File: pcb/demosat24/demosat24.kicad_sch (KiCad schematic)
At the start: 7 parts, among them J1 Power, J2 Digital/PWM, J3 Analog, J4 Digital/PWM, J5 Conn_01x04, J6 Conn_01x04, J7 Conn_01x02

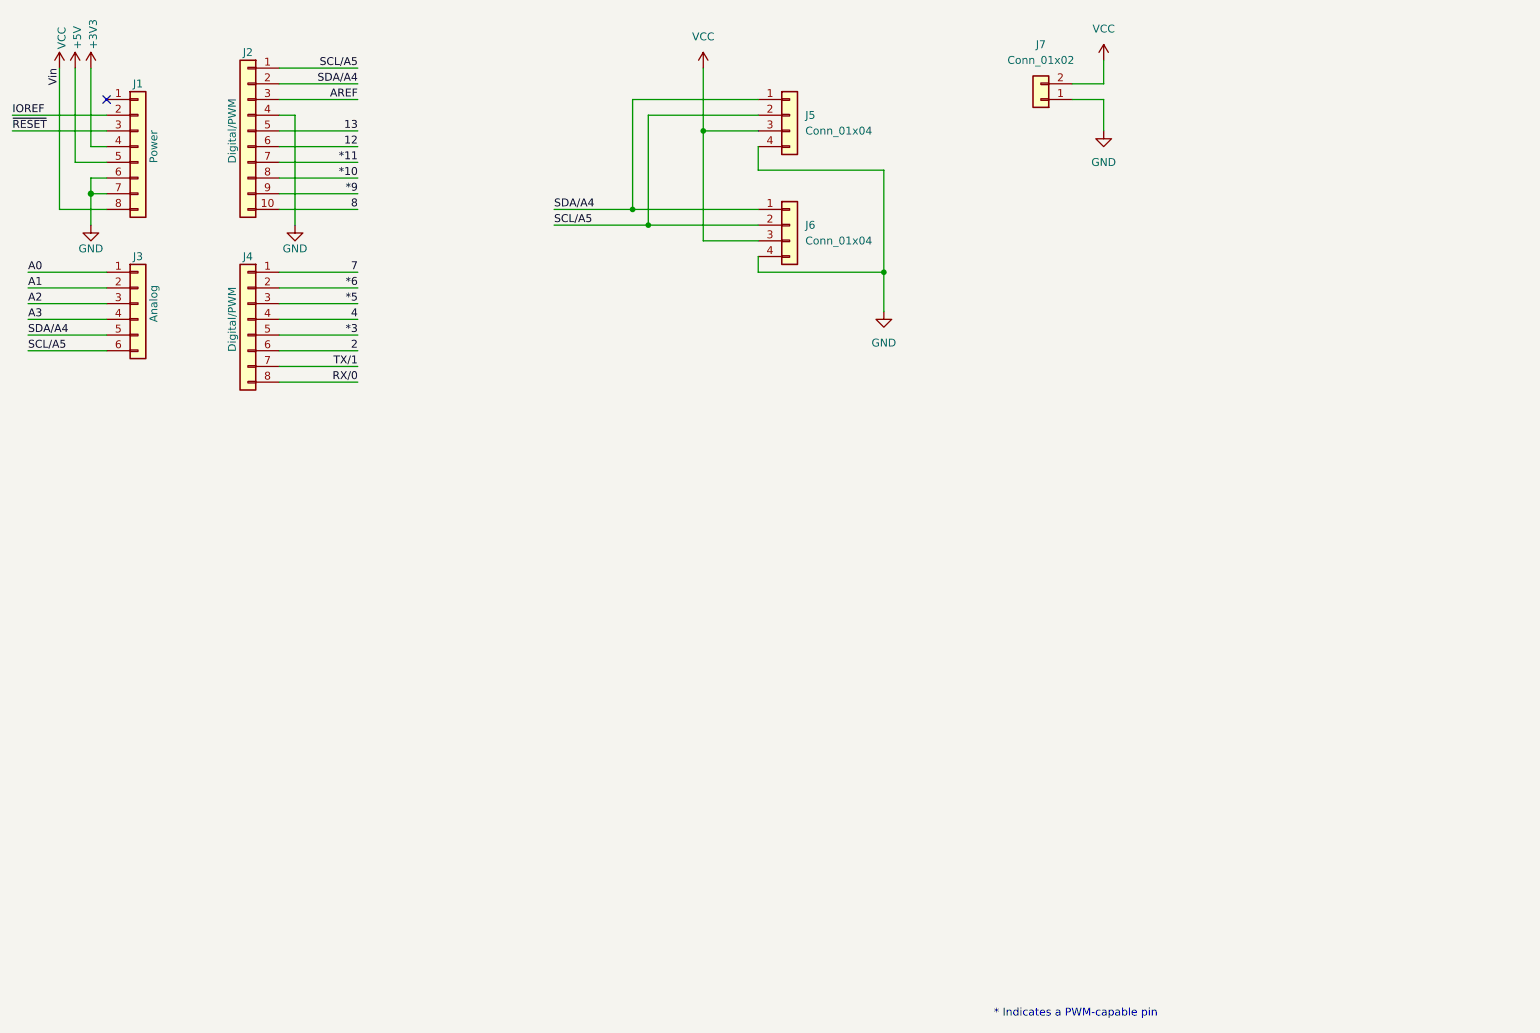
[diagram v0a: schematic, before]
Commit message: complete schematic added
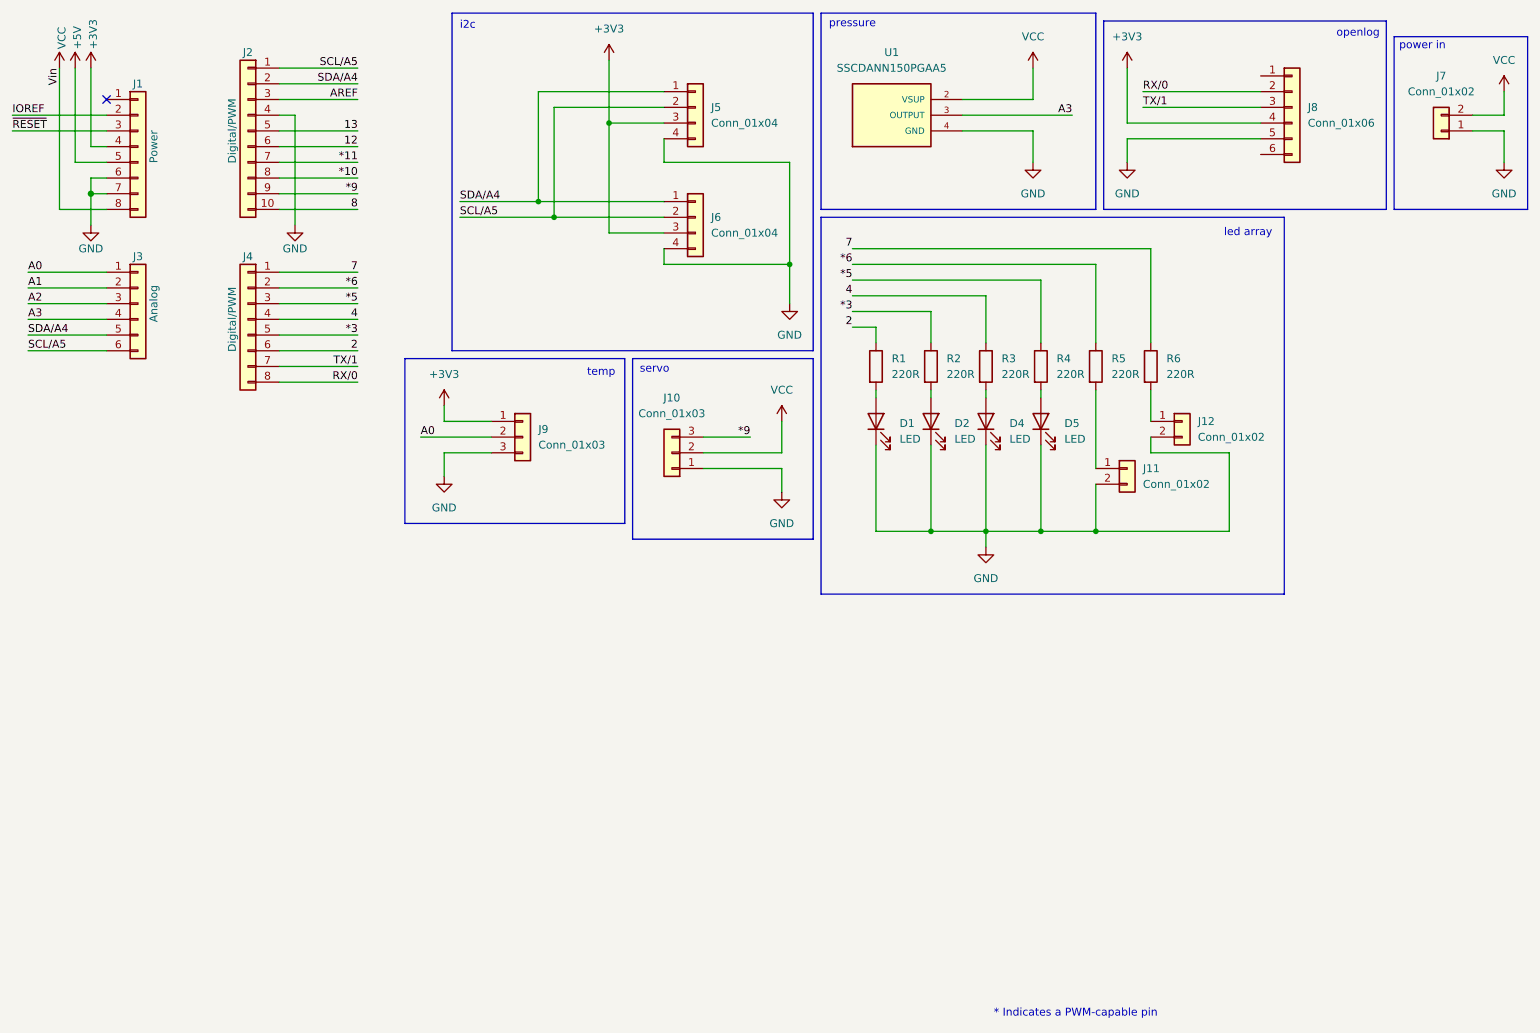
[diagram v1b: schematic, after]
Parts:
- added D1, D2, D4, D5: LED, LED_THT:LED_D5.0mm, symbol Device:LED
- added J10, J9: Conn_01x03, symbol Connector_Generic:Conn_01x03
- added J11, J12: Conn_01x02, Connector_PinHeader_2.54mm:PinHeader_1x02_P2.54mm_Vertical, symbol Connector_Generic:Conn_01x02
- added J8: Conn_01x06, Connector_PinSocket_2.54mm:PinSocket_1x06_P2.54mm_Vertical, symbol Connector_Generic:Conn_01x06
- added R1, R2, R3, R4, R5, R6: 220R, Resistor_THT:R_Axial_DIN0207_L6.3mm_D2.5mm_P10.16mm_Horizontal, symbol Device:R
- added U1: SSCDANN150PGAA5, SSCDANN150PGAA5:XDCR_SSCDANN150PGAA5, symbol SSCDANN150PGAA5:SSCDANN150PGAA5
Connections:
- net *3: now also R2.1
- net *5: now also R4.1
- net *6: now also R5.1
- net *9: now also J10.3 (Pin_3)
- net +3V3: now also J5.3 (Pin_3), J6.3 (Pin_3), J8.4 (Pin_4), J9.1 (Pin_1)
- net 2: now also R1.1
- net 4: now also R3.1
- net 7: now also R6.1
- net A0: now also J9.2 (Pin_2)
- net A3: now also U1.3 (OUTPUT)
- net GND: now also D1.1 (K), D2.1 (K), D4.1 (K), D5.1 (K), J10.1 (Pin_1), J11.2 (Pin_2), J12.2 (Pin_2), J8.5 (Pin_5), J9.3 (Pin_3), U1.4 (GND)
- net RX/0: now also J8.2 (Pin_2)
- net TX/1: now also J8.3 (Pin_3)
- net VCC: now also J10.2 (Pin_2), U1.2 (VSUP); no longer J5.3 (Pin_3), J6.3 (Pin_3)
- new net: J11.1 (Pin_1), R5.2
- new net: J12.1 (Pin_1), R6.2
- new net: D2.2 (A), R2.2
- new net: D5.2 (A), R4.2
- new net: D1.2 (A), R1.2
- new net: D4.2 (A), R3.2
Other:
- note added: "i2c"
- note added: "led array"
- note added: "openlog"
- note added: "power in"
- note added: "pressure"
- note added: "servo"
- note added: "temp"
- moved on the sheet: J5, J6, J7

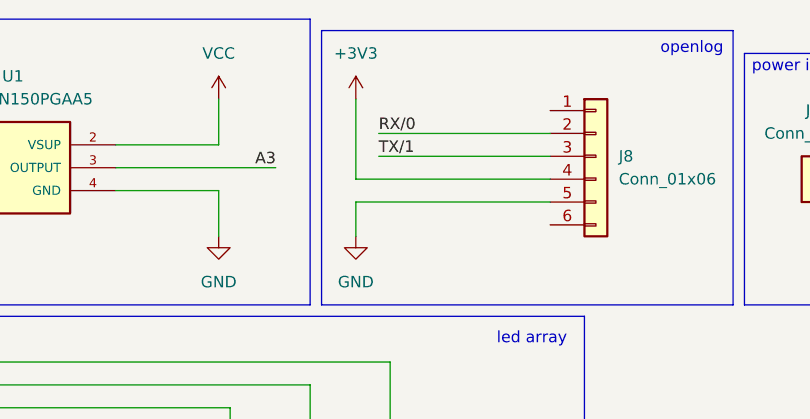
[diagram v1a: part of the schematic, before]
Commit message: pcb with one servo, all data and power connected but not ground
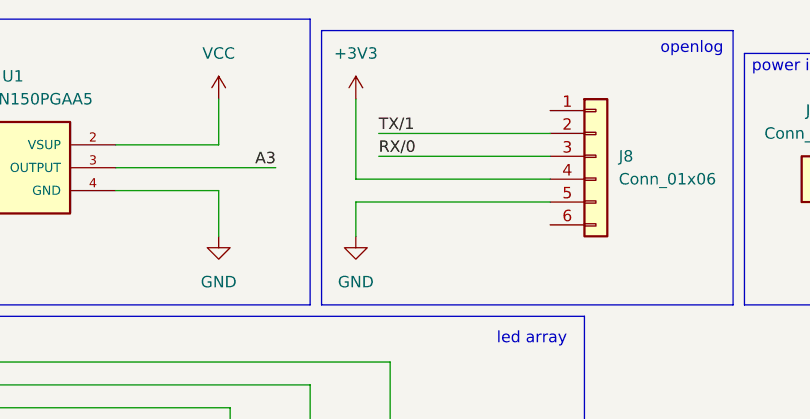
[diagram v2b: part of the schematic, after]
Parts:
- J10: footprint (none) -> Connector_PinHeader_2.54mm:PinHeader_1x03_P2.54mm_Vertical
- J7: footprint Connector_JST:JST_PH_B2B-PH-K_1x02_P2.00mm_Vertical -> Connector_JST:JST_XH_B2B-XH-A_1x02_P2.50mm_Vertical
- J9: footprint (none) -> Connector_Molex:Molex_SL_171971-0003_1x03_P2.54mm_Vertical
- R1, R2, R3, R4, R5, R6: footprint Resistor_THT:R_Axial_DIN0207_L6.3mm_D2.5mm_P10.16mm_Horizontal -> Resistor_THT:R_Axial_DIN0207_L6.3mm_D2.5mm_P7.62mm_Horizontal
- U1: footprint SSCDANN150PGAA5:XDCR_SSCDANN150PGAA5 -> libs:XDCR_SSCDANN150PGAA5
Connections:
- net RX/0: now also J8.3 (Pin_3); no longer J8.2 (Pin_2)
- net TX/1: now also J8.2 (Pin_2); no longer J8.3 (Pin_3)

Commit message: minor changes to pcb
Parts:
- J7: footprint Connector_JST:JST_XH_B2B-XH-A_1x02_P2.50mm_Vertical -> Connector_JST:JST_PH_B2B-PH-K_1x02_P2.00mm_Vertical
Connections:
- net A0: now also U1.3 (OUTPUT); no longer J9.2 (Pin_2)
- net A3: now also J9.2 (Pin_2); no longer U1.3 (OUTPUT)
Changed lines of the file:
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@@
 	(wire
 		(pts
-			(xy 96.52 86.36) (xy 85.09 86.36)
+			(xy 96.52 86.36) (xy 86.36 86.36)
 		)
 		(stroke
@@
 	)
 	(label "A3"
+		(at 86.36 86.36 180)
+		(fields_autoplaced yes)
+		(effects
+			(font
+				(size 1.27 1.27)
+			)
+			(justify right bottom)
+		)
+	)
+	(label "A3"
 		(at 21.59 67.31 0)
 		(fields_autoplaced yes)
@@
 		)
 	)
+	(label "A0"
+		(at 190.5 34.29 0)
+		(fields_autoplaced yes)
+		(effects
+			(font
+				(size 1.27 1.27)
+			)
+			(justify left bottom)
+		)
+	)
 	(label "*10"
 		(at 74.93 44.45 180)
@@
 		)
 	)
-	(label "A0"
-		(at 85.09 86.36 0)
-		(fields_autoplaced yes)
-		(effects
-			(font
-				(size 1.27 1.27)
-			)
-			(justify left bottom)
-		)
-	)
 	(label "*11"
 		(at 74.93 41.91 180)
@@
 	(label "TX{slash}1"
 		(at 74.93 74.93 180)
-		(fields_autoplaced yes)
-		(effects
-			(font
-				(size 1.27 1.27)
-			)
-			(justify right bottom)
-		)
-	)
-	(label "A3"
-		(at 190.5 34.29 180)
 		(fields_autoplaced yes)
 		(effects
@@
 			)
 		)
-		(property "Footprint" "Connector_JST:JST_XH_B2B-XH-A_1x02_P2.50mm_Vertical"
+		(property "Footprint" "Connector_JST:JST_PH_B2B-PH-K_1x02_P2.00mm_Vertical"
 			(at 250.19 36.83 0)
 			(effects

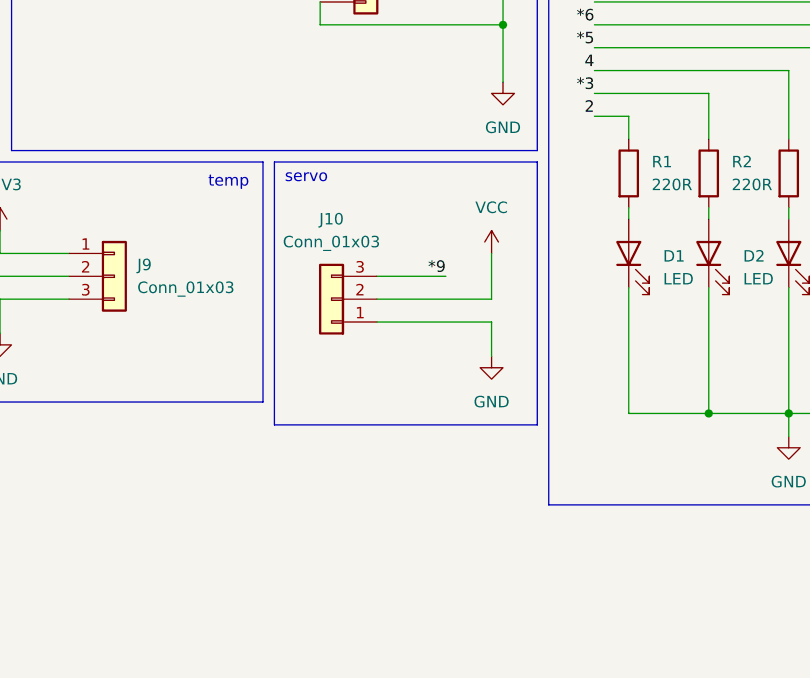
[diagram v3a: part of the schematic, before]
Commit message: PCB Ordered! switched to dual layer board with ground plane added headers for a second servo cleaned up repo
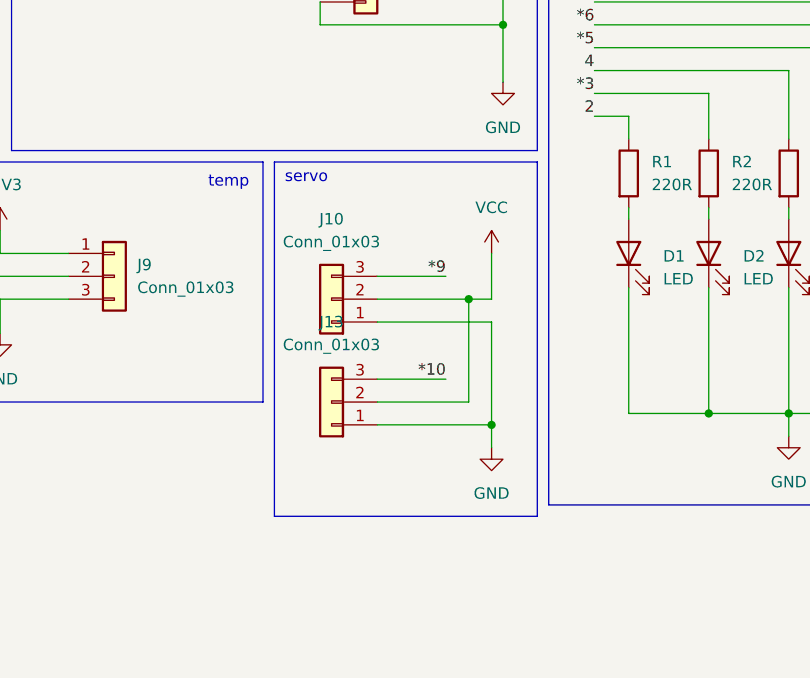
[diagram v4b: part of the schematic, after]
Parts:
- added J13: Conn_01x03, Connector_PinHeader_2.54mm:PinHeader_1x03_P2.54mm_Vertical, symbol Connector_Generic:Conn_01x03
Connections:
- net *10: now also J13.3 (Pin_3)
- net GND: now also J13.1 (Pin_1)
- net VCC: now also J13.2 (Pin_2)
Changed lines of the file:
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@@
 	)
 	(junction
+		(at 143.51 102.87)
+		(diameter 0)
+		(color 0 0 0 0)
+	)
+	(junction
 		(at 106.68 50.8)
 		(diameter 0)
@@
 		(color 0 0 0 0)
 	)
+	(junction
+		(at 140.97 88.9)
+		(diameter 0)
+		(color 0 0 0 0)
+	)
 	(no_connect
 		(at 34.29 31.75)
@@
 	(wire
 		(pts
+			(xy 143.51 102.87) (xy 143.51 105.41)
+		)
+		(stroke
+			(width 0)
+			(type default)
+		)
+	)
+	(wire
+		(pts
 			(xy 91.44 48.26) (xy 104.14 48.26)
 		)
@@
 	(wire
 		(pts
+			(xy 130.81 100.33) (xy 140.97 100.33)
+		)
+		(stroke
+			(width 0)
+			(type default)
+		)
+	)
+	(wire
+		(pts
 			(xy 167.64 78.74) (xy 167.64 80.01)
 		)
@@
 	(wire
 		(pts
-			(xy 130.81 88.9) (xy 143.51 88.9)
+			(xy 130.81 88.9) (xy 140.97 88.9)
 		)
 		(stroke
@@
 	(wire
 		(pts
-			(xy 143.51 91.44) (xy 143.51 95.25)
+			(xy 143.51 91.44) (xy 143.51 102.87)
 		)
 		(stroke
@@
 	(wire
 		(pts
+			(xy 140.97 100.33) (xy 140.97 88.9)
+		)
+		(stroke
+			(width 0)
+			(type default)
+		)
+	)
+	(wire
+		(pts
+			(xy 140.97 88.9) (xy 143.51 88.9)
+		)
+		(stroke
+			(width 0)
+			(type default)
+		)
+	)
+	(wire
+		(pts
 			(xy 158.75 87.63) (xy 158.75 101.6)
 		)
@@
 	(wire
 		(pts
+			(xy 130.81 97.79) (xy 138.43 97.79)
+		)
+		(stroke
+			(width 0)
+			(type default)
+		)
+	)
+	(wire
+		(pts
 			(xy 62.23 72.39) (xy 74.93 72.39)
 		)
@@
 	(wire
 		(pts
+			(xy 130.81 102.87) (xy 143.51 102.87)
+		)
+		(stroke
+			(width 0)
+			(type default)
+		)
+	)
+	(wire
+		(pts
 			(xy 154.94 66.04) (xy 167.64 66.04)
 		)
@@
 	(rectangle
 		(start 119.38 73.66)
-		(end 148.59 102.87)
+		(end 148.59 113.03)
 		(stroke
 			(width 0)
@@
 		)
 	)
+	(label "*10"
+		(at 138.43 97.79 180)
+		(fields_autoplaced yes)
+		(effects
+			(font
+				(size 1.27 1.27)
+			)
+			(justify right bottom)
+		)
+	)
 	(label "*9"
 		(at 138.43 86.36 180)
@@
 		(lib_name "GND_6")
 		(lib_id "power:GND")
-		(at 143.51 95.25 0)
+		(at 143.51 105.41 0)
 		(unit 1)
 		(exclude_from_sim no)
@@
 		(fields_autoplaced yes)
 		(property "Reference" "#PWR016"
-			(at 143.51 101.6 0)
+			(at 143.51 111.76 0)
 			(effects
 				(font
@@
 		)
 		(property "Value" "GND"
-			(at 143.51 100.33 0)
+			(at 143.51 110.49 0)
 			(effects
 				(font
@@
 		)
 		(property "Footprint" ""
-			(at 143.51 95.25 0)
+			(at 143.51 105.41 0)
 			(effects
 				(font
@@
 		)
 		(property "Datasheet" ""
-			(at 143.51 95.25 0)
+			(at 143.51 105.41 0)
 			(effects
 				(font
@@
 		)
 		(property "Description" "Power symbol creates a global label with name \"GND\" , ground"
-			(at 143.51 95.25 0)
+			(at 143.51 105.41 0)
 			(effects
 				(font
@@
 					(unit 1)
 				)
+			)
+		)
+	)
+	(symbol
+		(lib_id "Connector_Generic:Conn_01x03")
+		(at 125.73 100.33 180)
+		(unit 1)
+		(exclude_from_sim no)
+		(in_bom yes)
+		(on_board yes)
+		(dnp no)
+		(fields_autoplaced yes)
+		(property "Reference" "J13"
+			(at 125.73 91.44 0)
+			(effects
+				(font
+					(size 1.27 1.27)
+				)
+			)
+		)
+		(property "Value" "Conn_01x03"
+			(at 125.73 93.98 0)
+			(effects
+				(font
+					(size 1.27 1.27)
+				)
+			)
+		)
+		(property "Footprint" "Connector_PinHeader_2.54mm:PinHeader_1x03_P2.54mm_Vertical"
+			(at 125.73 100.33 0)
+			(effects
+				(font
+					(size 1.27 1.27)
+				)
+				(hide yes)
+			)
+		)
+		(property "Datasheet" "~"
+			(at 125.73 100.33 0)
+			(effects
+				(font
+					(size 1.27 1.27)
+				)
+				(hide yes)
+			)
+		)
+		(property "Description" "Generic connector, single row, 01x03, script generated (kicad-library-utils/schlib/autogen/connector/)"
+			(at 125.73 100.33 0)
+			(effects
+				(font
+					(size 1.27 1.27)
+				)
+				(hide yes)
+			)
+		)
+		(pin "1"
+		)
+		(pin "3"
+		)
+		(pin "2"
+		)
+		(instances
+			(project "demosat24"
+				(path "/e63e39d7-6ac0-4ffd-8aa3-1841a4541b55"
+					(reference "J13")
+					(unit 1)
+				)

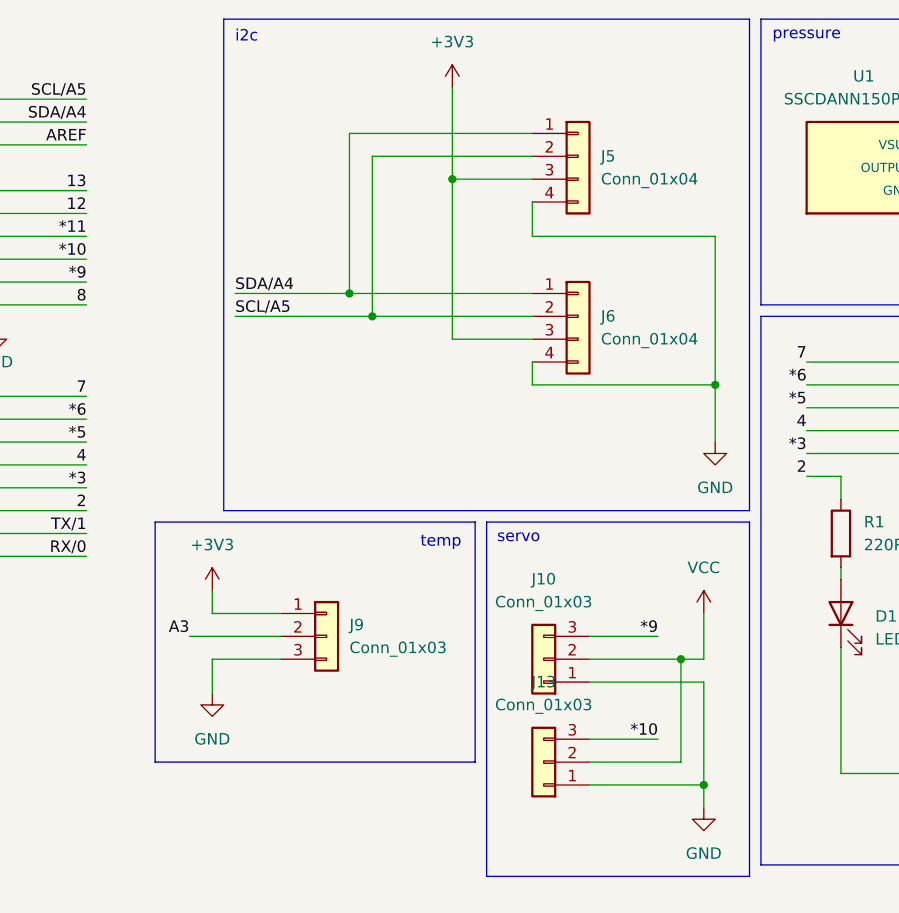
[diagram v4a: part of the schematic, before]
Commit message: updated pcb design with information learned from assembling the board
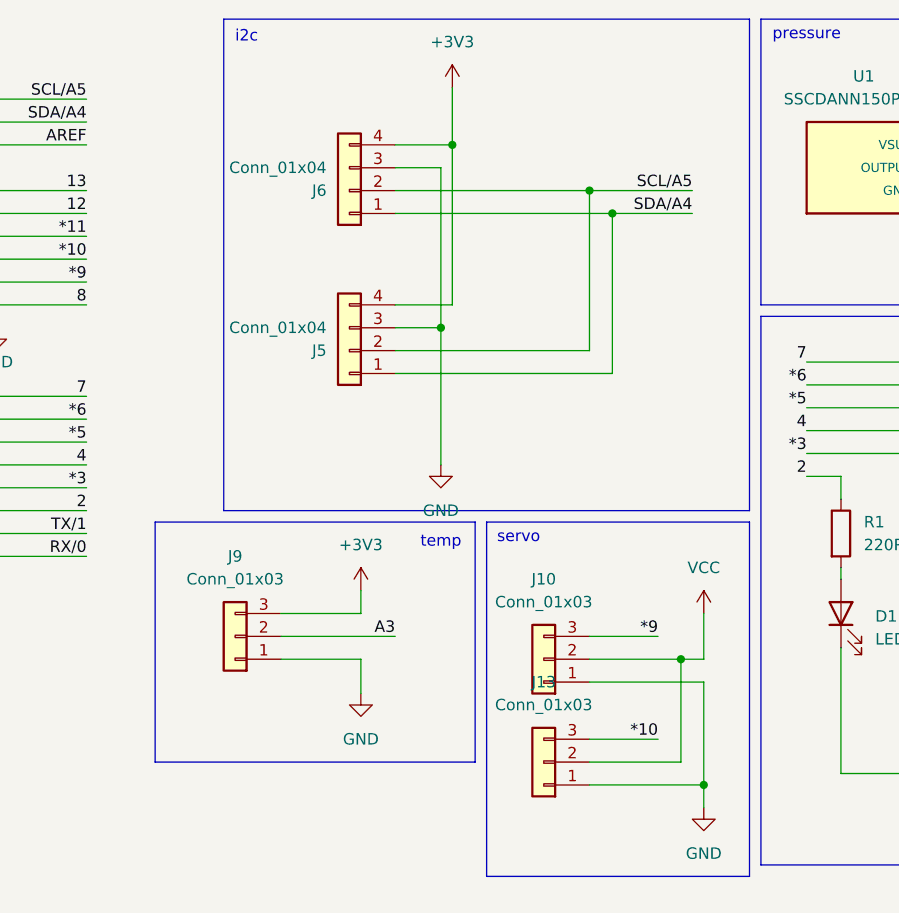
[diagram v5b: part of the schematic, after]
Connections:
- net +3V3: now also J5.4 (Pin_4), J6.4 (Pin_4), J9.3 (Pin_3); no longer J5.3 (Pin_3), J6.3 (Pin_3), J9.1 (Pin_1)
- net GND: now also J5.3 (Pin_3), J6.3 (Pin_3), J9.1 (Pin_1); no longer J5.4 (Pin_4), J6.4 (Pin_4), J9.3 (Pin_3)
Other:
- moved on the sheet: J5, J6, J9
